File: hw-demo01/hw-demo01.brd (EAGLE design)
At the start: 61.9 x 63.5 mm, 37 parts, among them IC3 MCP2562T, IC4 STM32F042

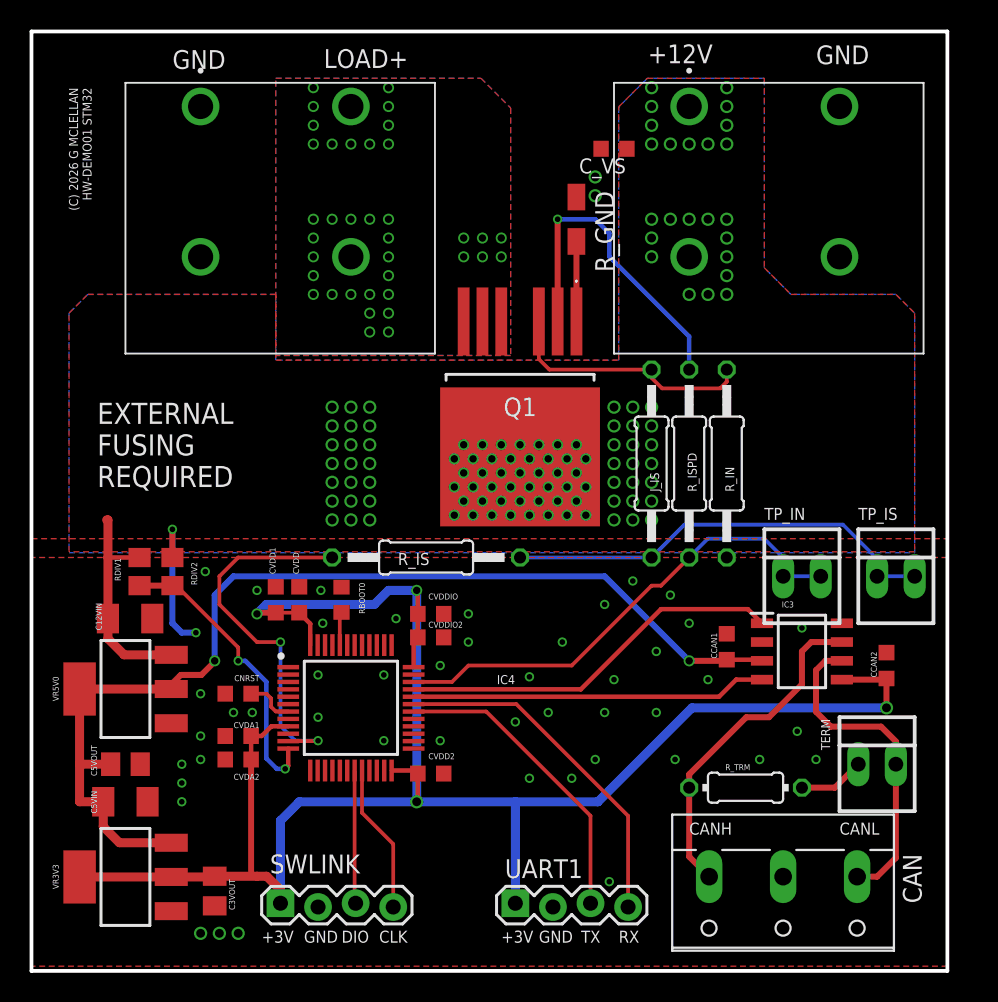
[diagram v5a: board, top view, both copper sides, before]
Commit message: tweak board dimensions
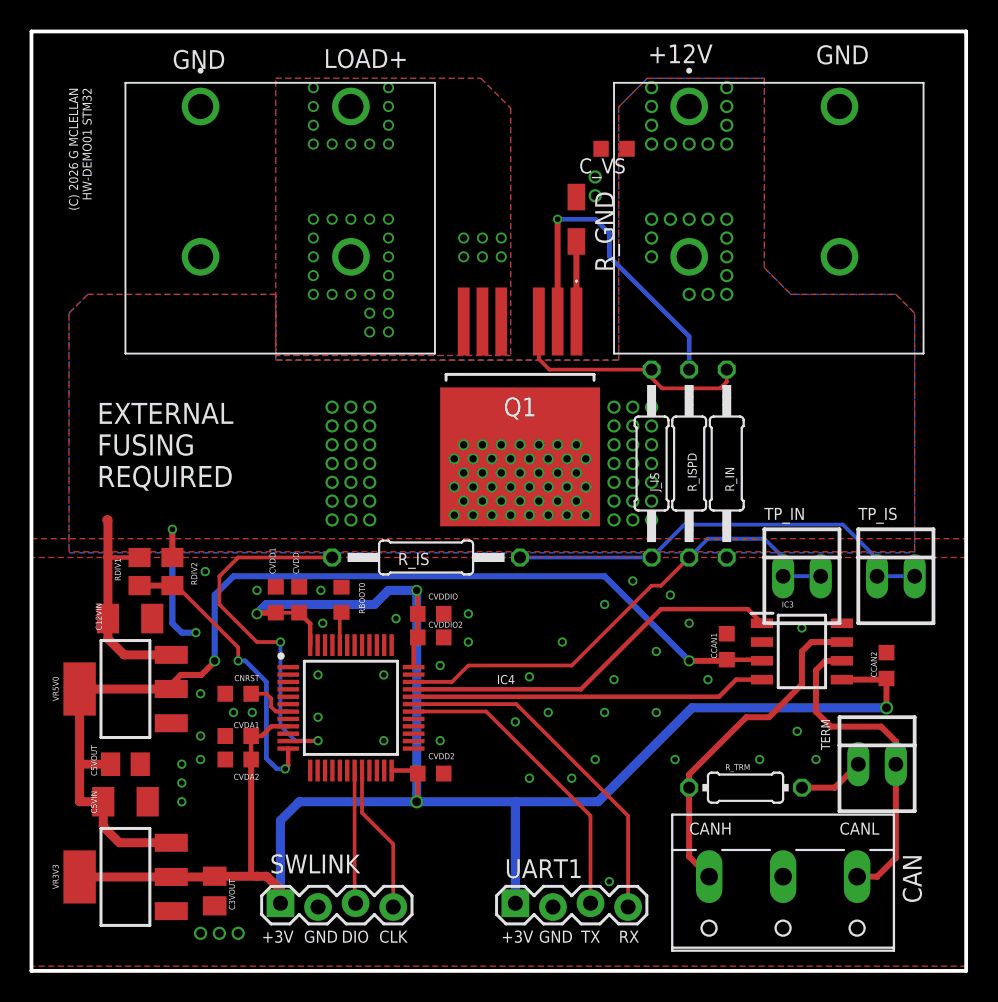
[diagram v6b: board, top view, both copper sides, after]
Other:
- board size 61.9 x 63.5 mm -> 63.2 x 63.5 mm
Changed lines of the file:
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@@
 <board>
 <plain>
-<wire x1="1.27" y1="0" x2="63.17" y2="0" width="0.254" layer="20"/>
-<wire x1="63.17" y1="0" x2="63.17" y2="63.49" width="0.254" layer="20"/>
-<wire x1="63.17" y1="63.49" x2="1.27" y2="63.49" width="0.254" layer="20"/>
+<wire x1="1.27" y1="0" x2="64.44" y2="0" width="0.254" layer="20"/>
+<wire x1="64.44" y1="0" x2="64.44" y2="63.49" width="0.254" layer="20"/>
+<wire x1="64.44" y1="63.49" x2="1.27" y2="63.49" width="0.254" layer="20"/>
 <wire x1="1.27" y1="63.49" x2="1.27" y2="0" width="0.254" layer="20"/>
 <text x="5.715" y="32.7025" size="1.4224" layer="25" font="vector" ratio="14">EXTERNAL
@@
 <polygon width="0.4064" layer="16" spacing="0.3048" rank="6">
 <vertex x="1.27" y="63.5"/>
-<vertex x="63.1825" y="63.5"/>
-<vertex x="63.1825" y="0"/>
+<vertex x="64.4525" y="63.5"/>
+<vertex x="64.4525" y="0"/>
 <vertex x="1.27" y="0"/>
 </polygon>
 <polygon width="0.4064" layer="1" spacing="0.3048" rank="6">
 <vertex x="1.27" y="63.5"/>
-<vertex x="63.1825" y="63.5"/>
-<vertex x="63.1825" y="27.94"/>
+<vertex x="64.4525" y="63.5"/>
+<vertex x="64.4525" y="27.94"/>
 <vertex x="1.27" y="27.94"/>
 </polygon>
@@
 <polygon width="0.254" layer="1" rank="5">
 <vertex x="1.27" y="29.21"/>
-<vertex x="63.1825" y="29.21"/>
-<vertex x="63.1825" y="0.3175"/>
+<vertex x="64.4525" y="29.21"/>
+<vertex x="64.4525" y="0.3175"/>
 <vertex x="1.27" y="0.3175"/>
 </polygon>

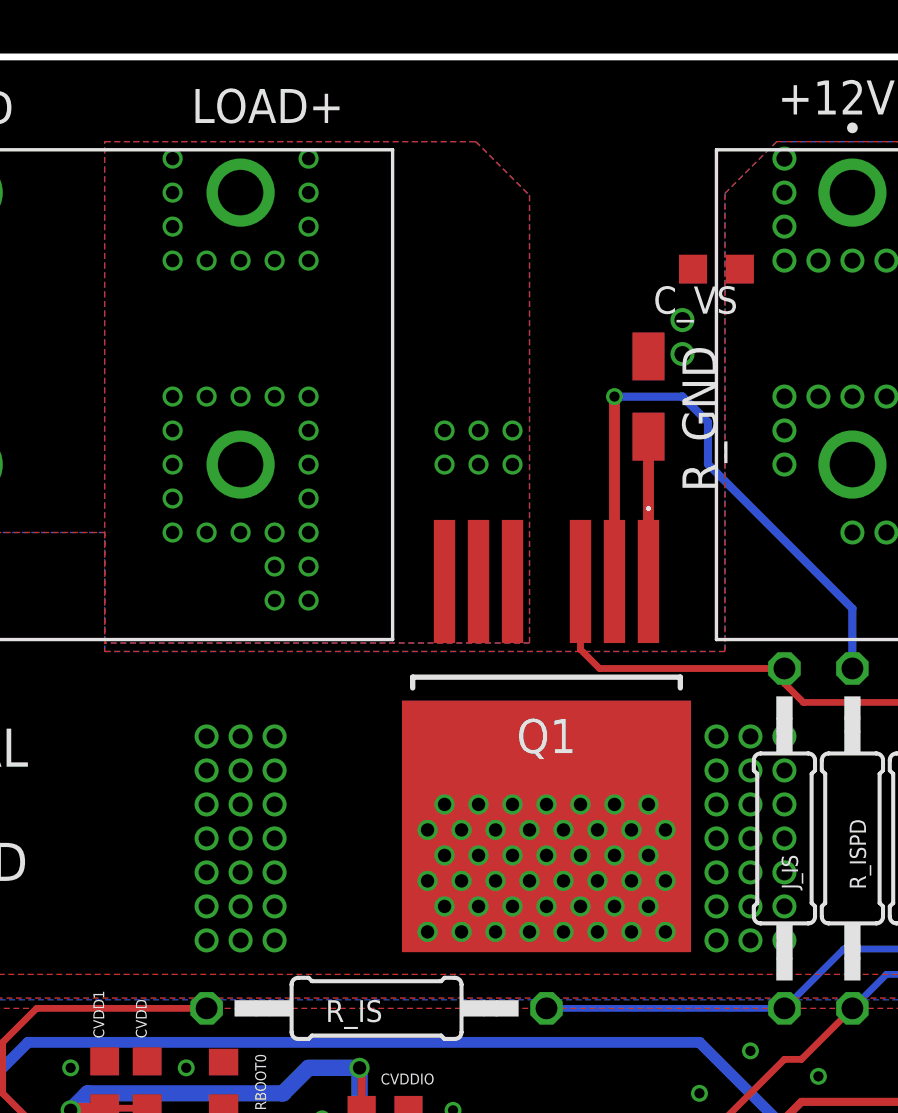
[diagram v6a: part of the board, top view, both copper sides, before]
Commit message: fix some via placement and drill sizes
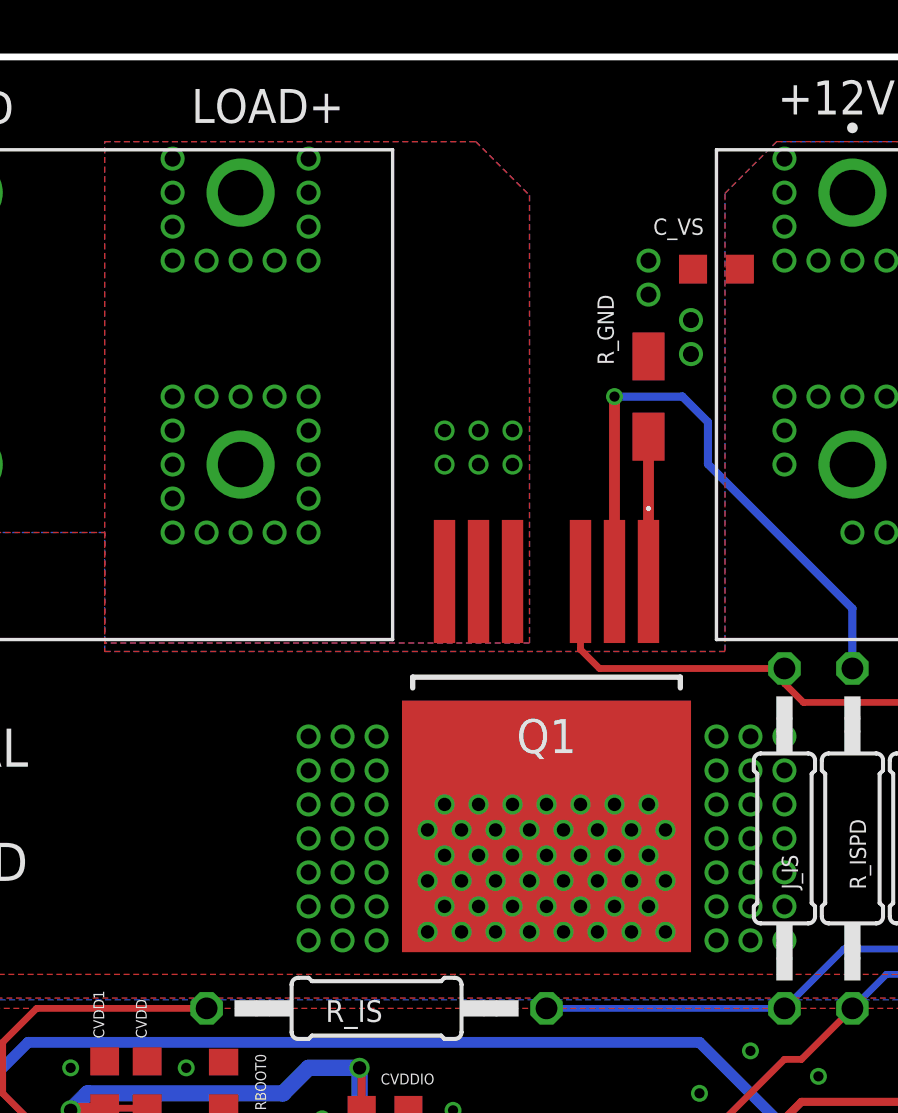
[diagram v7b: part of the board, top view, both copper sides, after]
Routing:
- net GND: vias 50 -> 52
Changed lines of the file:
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@@
 <attribute name="VALUE" x="50.8" y="21.59" size="1.016" layer="27" ratio="10"/>
 </element>
-<element name="R_GND" library="rcl" package="R1206W" value="0R0" x="38.1" y="50.8" rot="R270"/>
+<element name="R_GND" library="rcl" package="R1206W" value="0R0" x="38.1" y="50.8" smashed="yes" rot="R270">
+<attribute name="NAME" x="36.195" y="54.61" size="0.6096" layer="25" font="vector" ratio="14" rot="R270"/>
+</element>
 <element name="R_IS" library="rcl" package="0207/12" value="10K" x="27.94" y="27.94" smashed="yes" rot="R180">
 <attribute name="NAME" x="26.035" y="27.432" size="0.8128" layer="25" ratio="14"/>
@@
 <attribute name="MOUSER_PART_NUMBER" value="726-BTS500101TADATM2" x="34.29" y="37.465" size="1.778" layer="27" rot="R180" display="off"/>
 </element>
-<element name="C_VS" library="rcl" package="C0603K" value="100n" x="40.64" y="55.5625" rot="R180"/>
+<element name="C_VS" library="rcl" package="C0603K" value="100n" x="40.64" y="55.5625" smashed="yes" rot="R180">
+<attribute name="NAME" x="40.17" y="57.4525" size="0.6096" layer="25" font="vector" ratio="14" rot="R180"/>
+</element>
 </elements>
 <signals>
@@
 <vertex x="17.78" y="41.5925"/>
 </polygon>
-<via x="25.4" y="44.45" extent="1-16" drill="0.5"/>
-<via x="25.4" y="45.72" extent="1-16" drill="0.5"/>
-<via x="25.4" y="46.99" extent="1-16" drill="0.5"/>
-<via x="25.4" y="48.26" extent="1-16" drill="0.5"/>
+<wire x1="25.4" y1="44.45" x2="25.4" y2="44.45" width="0" layer="19" extent="1-16"/>
+<via x="25.4" y="45.72" extent="1-16" drill="0.6"/>
+<via x="25.4" y="46.99" extent="1-16" drill="0.6"/>
+<via x="25.4" y="48.26" extent="1-16" drill="0.6"/>
 <via x="30.48" y="48.26" extent="1-16" drill="0.5"/>
 <via x="31.75" y="48.26" extent="1-16" drill="0.5"/>
@@
 <via x="31.75" y="49.53" extent="1-16" drill="0.5"/>
 <via x="30.48" y="49.53" extent="1-16" drill="0.5"/>
-<via x="25.4" y="49.53" extent="1-16" drill="0.5"/>
-<via x="24.13" y="45.72" extent="1-16" drill="0.5"/>
-<via x="24.13" y="44.45" extent="1-16" drill="0.5"/>
-<via x="22.86" y="45.72" extent="1-16" drill="0.5"/>
-<via x="24.13" y="43.18" extent="1-16" drill="0.5"/>
-<via x="25.4" y="43.18" extent="1-16" drill="0.5"/>
-<via x="25.4" y="50.8" extent="1-16" drill="0.5"/>
-<via x="24.13" y="50.8" extent="1-16" drill="0.5"/>
-<via x="22.86" y="50.8" extent="1-16" drill="0.5"/>
-<via x="21.59" y="50.8" extent="1-16" drill="0.5"/>
-<via x="21.59" y="45.72" extent="1-16" drill="0.5"/>
-<via x="25.4" y="55.88" extent="1-16" drill="0.5"/>
-<via x="25.4" y="57.15" extent="1-16" drill="0.5"/>
-<via x="25.4" y="58.42" extent="1-16" drill="0.5"/>
-<via x="25.4" y="59.69" extent="1-16" drill="0.5"/>
-<via x="21.59" y="55.88" extent="1-16" drill="0.5"/>
-<via x="22.86" y="55.88" extent="1-16" drill="0.5"/>
-<via x="24.13" y="55.88" extent="1-16" drill="0.5"/>
-<via x="20.32" y="45.72" extent="1-16" drill="0.5"/>
-<via x="20.32" y="46.99" extent="1-16" drill="0.5"/>
-<via x="20.32" y="48.26" extent="1-16" drill="0.5"/>
-<via x="20.32" y="49.53" extent="1-16" drill="0.5"/>
-<via x="20.32" y="50.8" extent="1-16" drill="0.5"/>
-<via x="20.32" y="55.88" extent="1-16" drill="0.5"/>
-<via x="20.32" y="57.15" extent="1-16" drill="0.5"/>
-<via x="20.32" y="58.42" extent="1-16" drill="0.5"/>
-<via x="20.32" y="59.69" extent="1-16" drill="0.5"/>
+<via x="25.4" y="49.53" extent="1-16" drill="0.6"/>
+<via x="24.13" y="45.72" extent="1-16" drill="0.6"/>
+<wire x1="24.13" y1="44.45" x2="24.13" y2="44.45" width="0" layer="19" extent="1-16"/>
+<via x="22.86" y="45.72" extent="1-16" drill="0.6"/>
+<wire x1="24.13" y1="43.18" x2="24.13" y2="43.18" width="0" layer="19" extent="1-16"/>
+<wire x1="25.4" y1="43.18" x2="25.4" y2="43.18" width="0" layer="19" extent="1-16"/>
+<via x="25.4" y="50.8" extent="1-16" drill="0.6"/>
+<via x="24.13" y="50.8" extent="1-16" drill="0.6"/>
+<via x="22.86" y="50.8" extent="1-16" drill="0.6"/>
+<via x="21.59" y="50.8" extent="1-16" drill="0.6"/>
+<via x="21.59" y="45.72" extent="1-16" drill="0.6"/>
+<via x="25.4" y="55.88" extent="1-16" drill="0.6"/>
+<via x="25.4" y="57.15" extent="1-16" drill="0.6"/>
+<via x="25.4" y="58.42" extent="1-16" drill="0.6"/>
+<via x="25.4" y="59.69" extent="1-16" drill="0.6"/>
+<via x="21.59" y="55.88" extent="1-16" drill="0.6"/>
+<via x="22.86" y="55.88" extent="1-16" drill="0.6"/>
+<via x="24.13" y="55.88" extent="1-16" drill="0.6"/>
+<via x="20.32" y="45.72" extent="1-16" drill="0.6"/>
+<via x="20.32" y="46.99" extent="1-16" drill="0.6"/>
+<via x="20.32" y="48.26" extent="1-16" drill="0.6"/>
+<via x="20.32" y="49.53" extent="1-16" drill="0.6"/>
+<via x="20.32" y="50.8" extent="1-16" drill="0.6"/>
+<via x="20.32" y="55.88" extent="1-16" drill="0.6"/>
+<via x="20.32" y="57.15" extent="1-16" drill="0.6"/>
+<via x="20.32" y="58.42" extent="1-16" drill="0.6"/>
+<via x="20.32" y="59.69" extent="1-16" drill="0.6"/>
 <contactref element="Q1" pad="5"/>
 <contactref element="Q1" pad="7"/>
@@
 <contactref element="LOAD+" pad="1_2"/>
 <contactref element="LOAD+" pad="1_1"/>
-<via x="39.37" y="52.3875" extent="1-16" drill="0.6"/>
-<via x="39.37" y="53.6575" extent="1-16" drill="0.6"/>
+<via x="39.6875" y="52.3875" extent="1-16" drill="0.6"/>
+<via x="39.6875" y="53.6575" extent="1-16" drill="0.6"/>
 <polygon width="0.254" layer="1" rank="5">
 <vertex x="1.27" y="29.21"/>
@@
 <contactref element="C_VS" pad="2"/>
 <via x="28.8925" y="20.6375" extent="1-16" drill="0.381"/>
+<via x="38.1" y="54.61" extent="1-16" drill="0.6"/>
+<via x="38.1" y="55.88" extent="1-16" drill="0.6"/>
 </signal>
 <signal name="CANH">
@@
 <via x="43.18" y="36.83" extent="1-16" drill="0.6"/>
 <via x="43.18" y="38.1" extent="1-16" drill="0.6"/>
-<via x="24.13" y="30.48" extent="1-16" drill="0.6"/>
-<via x="22.86" y="30.48" extent="1-16" drill="0.6"/>
-<via x="21.59" y="30.48" extent="1-16" drill="0.6"/>
-<via x="21.59" y="31.75" extent="1-16" drill="0.6"/>
-<via x="22.86" y="31.75" extent="1-16" drill="0.6"/>
-<via x="24.13" y="31.75" extent="1-16" drill="0.6"/>
-<via x="24.13" y="33.02" extent="1-16" drill="0.6"/>
-<via x="22.86" y="33.02" extent="1-16" drill="0.6"/>
-<via x="21.59" y="33.02" extent="1-16" drill="0.6"/>
-<via x="21.59" y="34.29" extent="1-16" drill="0.6"/>
-<via x="22.86" y="34.29" extent="1-16" drill="0.6"/>
-<via x="24.13" y="34.29" extent="1-16" drill="0.6"/>
-<via x="24.13" y="35.56" extent="1-16" drill="0.6"/>
-<via x="22.86" y="35.56" extent="1-16" drill="0.6"/>
-<via x="21.59" y="35.56" extent="1-16" drill="0.6"/>
-<via x="21.59" y="36.83" extent="1-16" drill="0.6"/>
-<via x="22.86" y="36.83" extent="1-16" drill="0.6"/>
-<via x="24.13" y="36.83" extent="1-16" drill="0.6"/>
-<via x="24.13" y="38.1" extent="1-16" drill="0.6"/>
-<via x="22.86" y="38.1" extent="1-16" drill="0.6"/>
-<via x="21.59" y="38.1" extent="1-16" drill="0.6"/>
+<via x="27.94" y="30.48" extent="1-16" drill="0.6"/>
+<via x="26.67" y="30.48" extent="1-16" drill="0.6"/>
+<via x="25.4" y="30.48" extent="1-16" drill="0.6"/>
+<via x="25.4" y="31.75" extent="1-16" drill="0.6"/>
+<via x="26.67" y="31.75" extent="1-16" drill="0.6"/>
+<via x="27.94" y="31.75" extent="1-16" drill="0.6"/>
+<via x="27.94" y="33.02" extent="1-16" drill="0.6"/>
+<via x="26.67" y="33.02" extent="1-16" drill="0.6"/>
+<via x="25.4" y="33.02" extent="1-16" drill="0.6"/>
+<via x="25.4" y="34.29" extent="1-16" drill="0.6"/>
+<via x="26.67" y="34.29" extent="1-16" drill="0.6"/>
+<via x="27.94" y="34.29" extent="1-16" drill="0.6"/>
+<via x="27.94" y="35.56" extent="1-16" drill="0.6"/>
+<via x="26.67" y="35.56" extent="1-16" drill="0.6"/>
+<via x="25.4" y="35.56" extent="1-16" drill="0.6"/>
+<via x="25.4" y="36.83" extent="1-16" drill="0.6"/>
+<via x="26.67" y="36.83" extent="1-16" drill="0.6"/>
+<via x="27.94" y="36.83" extent="1-16" drill="0.6"/>
+<via x="27.94" y="38.1" extent="1-16" drill="0.6"/>
+<via x="26.67" y="38.1" extent="1-16" drill="0.6"/>
+<via x="25.4" y="38.1" extent="1-16" drill="0.6"/>
 <via x="44.45" y="55.88" extent="1-16" drill="0.6"/>
 <via x="45.72" y="55.88" extent="1-16" drill="0.6"/>
